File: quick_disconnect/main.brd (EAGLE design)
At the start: 25.4 x 11.1 mm, 12 parts

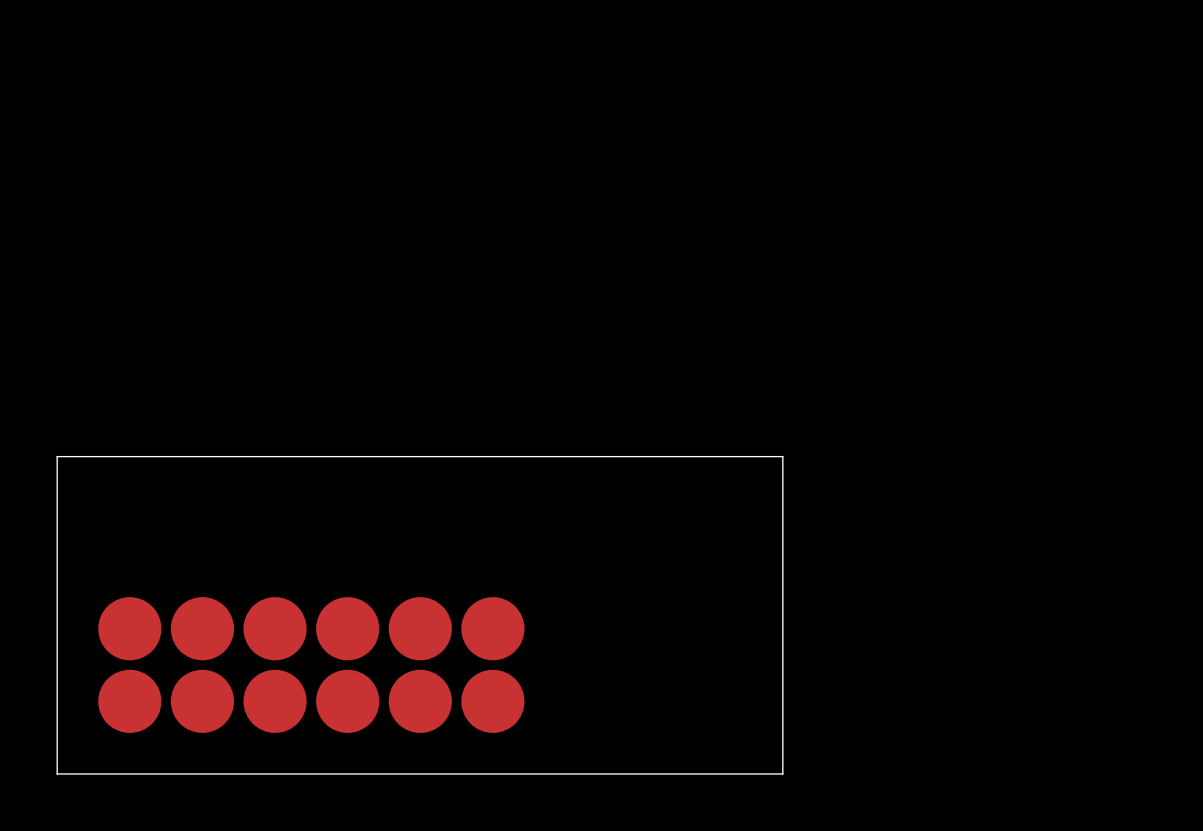
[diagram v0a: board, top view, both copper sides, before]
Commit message: initial design of 4x 2pin molex, 1x 16 pin molex, 4 header acc
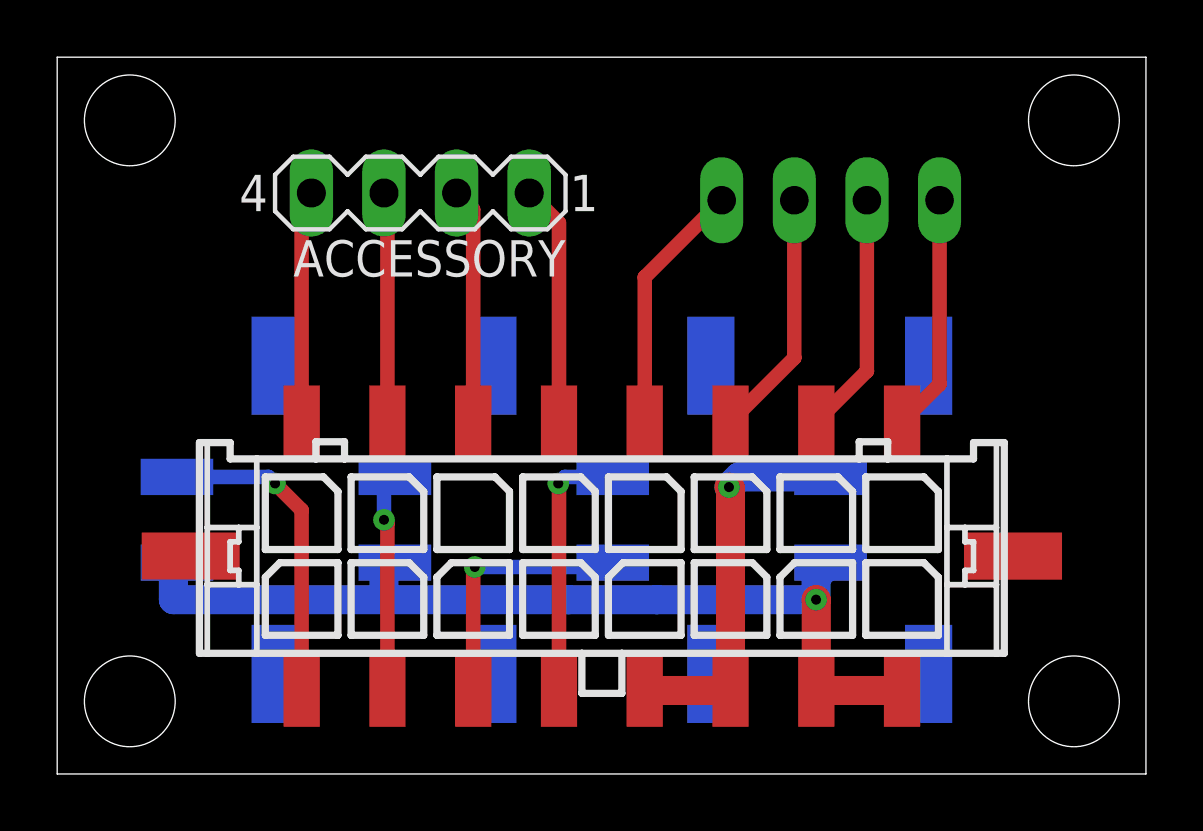
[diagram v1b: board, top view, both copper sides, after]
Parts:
- removed U$1, U$10, U$11, U$12, U$2, U$3, U$4, U$5, U$6, U$7, U$8, U$9: PRECI-DIP_90022-AS, eric_personal_parts:PRECI-DIP_90022-AS
- added ACCESSORY: (no value), con-lstb:MA04-1
- added HEATER, HOTEND_FAN, PCF, THERMISTOR: (no value), con-molex-micro-fit-3_0:43650-0224
- added STEPPER: 22-23-2041, con-molex:22-23-2041
- added X1: (no value), con-molex-micro-fit-3_0:43045-1618
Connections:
- new net ACCESSORY_1: ACCESSORY.1, X1.P$4
- new net ACCESSORY_2: ACCESSORY.2, X1.P$3
- new net ACCESSORY_3: ACCESSORY.3, X1.P$2
- new net ACCESSORY_4: ACCESSORY.4, X1.P$1
- net HEATER_GND: now also HEATER.P$2, X1.P$13, X1.P$14; no longer U$3.P$1, U$4.P$1
- net HOTEND_FAN_GND: now also HOTEND_FAN.P$2, X1.P$9; no longer U$8.P$1
- net PCF_GND: now also PCF.P$2, X1.P$10; no longer U$7.P$1
- net STEPPER_PHASE+2+: now also STEPPER.3, X1.P$6; no longer U$12.P$1
- net STEPPER_PHASE_1+: now also STEPPER.1, X1.P$8; no longer U$9.P$1
- net STEPPER_PHASE_1-: now also STEPPER.2, X1.P$7; no longer U$10.P$1
- net STEPPER_PHASE_2-: now also STEPPER.4, X1.P$5; no longer U$11.P$1
- net THERMISTOR_+: now also THERMISTOR.P$2, X1.P$12; no longer U$5.P$1
- net THERMISTOR_-: now also THERMISTOR.P$1, X1.P$11; no longer U$6.P$1
- net V+: now also HEATER.P$1, HOTEND_FAN.P$1, PCF.P$1, X1.P$15, X1.P$16; no longer U$1.P$1, U$2.P$1
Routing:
- net V+: track 0.00 -> 33.0 mm, vias 0 -> 1
- net HEATER_GND: track 0.00 -> 13.8 mm, vias 0 -> 1
- net HOTEND_FAN_GND: track 0.00 -> 11.2 mm, vias 0 -> 1
- net THERMISTOR_+: track 0.00 -> 9.25 mm, vias 0 -> 1
- net THERMISTOR_-: track 0.00 -> 9.23 mm, vias 0 -> 1
- net STEPPER_PHASE_2-: track 0.00 -> 8.86 mm
- net STEPPER_PHASE+2+: track 0.00 -> 8.67 mm
- net STEPPER_PHASE_1-: track 0.00 -> 8.48 mm
- net ACCESSORY_1: track 0.00 -> 8.43 mm
- net STEPPER_PHASE_1+: track 0.00 -> 8.29 mm
- net ACCESSORY_2: track 0.00 -> 8.24 mm
- net ACCESSORY_4: track 0.00 -> 8.14 mm
- net ACCESSORY_3: track 0.00 -> 8.05 mm
- net PCF_GND: track 0.00 -> 7.68 mm, vias 0 -> 1
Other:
- board size 25.4 x 11.1 mm -> 38.1 x 25.1 mm

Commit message: small routing updates
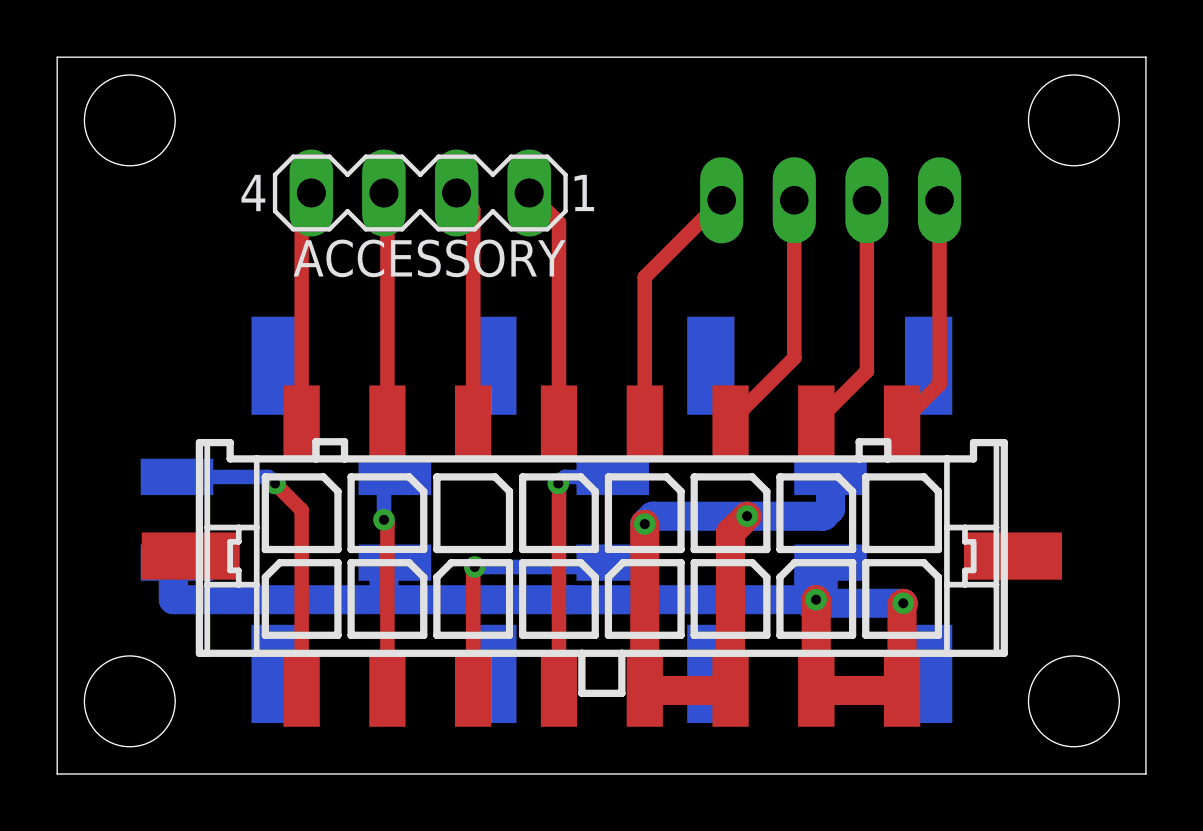
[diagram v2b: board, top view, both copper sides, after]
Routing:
- net HEATER_GND: track 13.8 -> 23.0 mm, vias 1 -> 2
- net V+: track 33.0 -> 39.1 mm, vias 1 -> 2
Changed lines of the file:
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@@
 <wire x1="26.55" y1="6.089" x2="26.543" y2="6.096" width="1.016" layer="1"/>
 <via x="26.543" y="6.096" extent="1-16" drill="0.35"/>
-<wire x1="26.543" y1="6.096" x2="26.543" y2="6.883" width="1.016" layer="16"/>
+<wire x1="26.543" y1="6.096" x2="26.543" y2="6.883" width="1.524" layer="16"/>
 <wire x1="26.543" y1="6.883" x2="27.05" y2="7.39" width="1.016" layer="16"/>
 <wire x1="26.55" y1="2.92" x2="29.55" y2="2.92" width="1.016" layer="1"/>
@@
 <wire x1="11.81" y1="7.39" x2="11.43" y2="7.01" width="1.016" layer="16"/>
 <wire x1="11.43" y1="7.01" x2="11.43" y2="6.096" width="1.016" layer="16"/>
+<wire x1="29.55" y1="2.92" x2="29.55" y2="5.928" width="1.016" layer="1"/>
+<wire x1="29.55" y1="5.928" x2="29.591" y2="5.969" width="1.016" layer="1"/>
+<via x="29.591" y="5.969" extent="1-16" drill="0.35"/>
+<wire x1="29.591" y1="5.969" x2="26.67" y2="5.969" width="1.016" layer="16"/>
+<wire x1="26.67" y1="5.969" x2="26.543" y2="6.096" width="1.016" layer="16"/>
 </signal>
 <signal name="HEATER_GND" class="1">
@@
 <contactref element="X1" pad="P$13"/>
 <contactref element="HEATER" pad="P$2"/>
-<wire x1="23.55" y1="2.92" x2="23.55" y2="9.978" width="1.016" layer="1"/>
-<wire x1="23.55" y1="9.978" x2="23.495" y2="10.033" width="1.016" layer="1"/>
-<via x="23.495" y="10.033" extent="1-16" drill="0.35"/>
-<wire x1="23.495" y1="10.033" x2="23.852" y2="10.39" width="1.016" layer="16"/>
-<wire x1="23.852" y1="10.39" x2="27.05" y2="10.39" width="1.016" layer="16"/>
 <wire x1="23.55" y1="2.92" x2="20.55" y2="2.92" width="1.016" layer="1"/>
+<wire x1="20.55" y1="2.92" x2="20.55" y2="8.739" width="1.016" layer="1"/>
+<wire x1="23.55" y1="2.92" x2="23.55" y2="8.437" width="1.016" layer="1"/>
+<wire x1="23.55" y1="8.437" x2="24.13" y2="9.017" width="1.016" layer="1"/>
+<via x="24.13" y="9.017" extent="1-16" drill="0.35"/>
+<via x="20.55" y="8.739" extent="1-16" drill="0.35"/>
+<wire x1="20.55" y1="8.739" x2="20.828" y2="9.017" width="1.016" layer="16"/>
+<wire x1="20.828" y1="9.017" x2="24.13" y2="9.017" width="1.016" layer="16"/>
+<wire x1="24.13" y1="9.017" x2="26.797" y2="9.017" width="1.016" layer="16"/>
+<wire x1="27.05" y1="9.27" x2="27.05" y2="10.39" width="1.016" layer="16"/>
+<wire x1="26.797" y1="9.017" x2="27.05" y2="9.27" width="1.016" layer="16"/>
 </signal>
 <signal name="THERMISTOR_+">
